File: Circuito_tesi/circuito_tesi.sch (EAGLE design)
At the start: 37 parts, among them IC1.8 317T, IC3.3 317T, IC5 317T, Q1 BSS138, U1 NRF52832, U2 SGP30, U3 MICS-6814, U4 OPA2277PA, U6 BME280, U7 LIS3DH

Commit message: Cambiate resistenze a 1/4 W max
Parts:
- removed Q1: BSS138, BSS138:BSS138
- removed R11: RMCF0603FT130R, Res_130OHM:RMCF0603FT130R
- removed R12: RMCF0603FT300R, Res_300OHM:RMCF0603FT300R
- added R8: ERA6VEB8200V, Res_820_0p25W:ERA6VEB8200V
- BT1, BT2, BT3, BT4: value BHX1-2450-SM -> 2996TR; device BHX1-2450-SM:BHX1-2450-SM -> Battery_holder:2996TR
- R1, R2: value RNCF0603BTE10K0 -> RNCP0805FTD10K0; device Res_10KOHM:RNCF0603BTE10K0 -> Res_10K_0p25W:RNCP0805FTD10K0
- R5: value RNCF0603BTE10K0 -> RP73PF2A130RBTDF; device Res_10KOHM:RNCF0603BTE10K0 -> Res_130_0p25:RP73PF2A130RBTDF
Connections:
- removed net N$8: R5.2
- net 5V: now also R5.2, R8.2; no longer R11.2, R9.2
- net GND: now also R9.1; no longer R12.1
- net N$11: now also R8.1; no longer R9.1
- net N$13: now also R5.1; no longer R11.1
- net N$9: now also R9.2; no longer R12.2
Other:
- moved on the sheet: BT1, BT2, BT3, BT4, R5, R9

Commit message: Aggiunte nuovi condensatori e voltage regulator
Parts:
- removed IC1.8, IC3.3, IC5: 317T, linear:317T
- added C7: GRM033C80J104KE15D, Condens_100nF:GRM033C80J104KE15D
- added C9: GRM033R60J103KA01D, Condens_10nF:GRM033R60J103KA01D
- added V_REG_1.8: MCP1825S-1802E/DB, V_Reg_1.8_SMD:MCP1825S-1802E/DB
- added V_REG_3.3: LD1117S33TR, V_Reg_3.3_SMD:LD1117S33TR
- added V_REG_5: LDL1117S50RSOT223_STM-L, V_Reg_5_SMD:LDL1117S50RSOT223_STM-L
- C1: value 10uF -> GRM033C80J104KE15D; device SparkFun-Capacitors:10UF-0805-10V-10% -> Condens_100nF:GRM033C80J104KE15D
- C2: value 10uF -> CL05A106MP5NUNC; device SparkFun-Capacitors:10UF-0805-10V-10% -> Condens_10uF:CL05A106MP5NUNC
- C3: value 0.33µF -> GRM035R60G475ME15D; device SparkFun-Capacitors:0.33UF/330NF-0805-50V-10% -> Condens_4.7uF:GRM035R60G475ME15D
- C4: value 0.1uF -> GRM033R60J105MEA2D; device SparkFun-Capacitors:0.1UF-0603-25V-5% -> Condens_1uF:GRM033R60J105MEA2D
- C5: value GRM033R60J103KA01D -> GRM033R60J105MEA2D; device Condens_10nF:GRM033R60J103KA01D -> Condens_1uF:GRM033R60J105MEA2D
- C6: value GRM033R60J103KA01D -> GRM035R60G475ME15D; device Condens_10nF:GRM033R60J103KA01D -> Condens_4.7uF:GRM035R60G475ME15D
- C8: value GRM033C80J104KE15D -> GRM033R60J103KA01D; device Condens_100nF:GRM033C80J104KE15D -> Condens_10nF:GRM033R60J103KA01D
- R5: value RP73PF2A130RBTDF -> RMCF0603FT5M10; device Res_130_0p25:RP73PF2A130RBTDF -> Res_5.1MOHM:RMCF0603FT5M10
- R7: value RMCF0603FT5M10 -> RP73PF2A130RBTDF; device Res_5.1MOHM:RMCF0603FT5M10 -> Res_130_0p25:RP73PF2A130RBTDF
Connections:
- net 1.8V: now also C5.2, C7.1, V_REG_1.8.VOUT; no longer C8.1, IC1.8.VO
- net 3.3: now also V_REG_3.3.OUT; no longer IC3.3.VO
- net 5V: now also C3.2, C6.2, R7.2, V_REG_1.8.VIN, V_REG_5.VOUT; no longer C4.1, IC5.VO, R5.2
- net GND: now also C1.1, C3.1, C4.1, C7.2, C8.1, C9.1, V_REG_1.8.GND_(TAB), V_REG_1.8.GND_(TAB)_2, V_REG_3.3.GND, V_REG_5.GND; no longer C1.2, C3.2, C4.2, C8.2, IC1.8.ADJ, IC3.3.ADJ, IC5.ADJ
- net N$13: now also R7.1; no longer R5.1
- net N$15: now also C9.2, R6.1; no longer C6.2, R7.1
- net N$17: now also C8.2, R5.2; no longer C5.2, R6.2
- net N$22: now also R5.1; no longer R6.1
- net N$7: now also R6.2; no longer R7.2
- net VDD: now also C1.2, C4.2, V_REG_3.3.IN, V_REG_5.VIN; no longer C1.1, C3.1, IC1.8.VI, IC3.3.VI, IC5.VI
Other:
- moved on the sheet: C1, C2, C3, C4, C5, C6, C8, R5, R6, R7

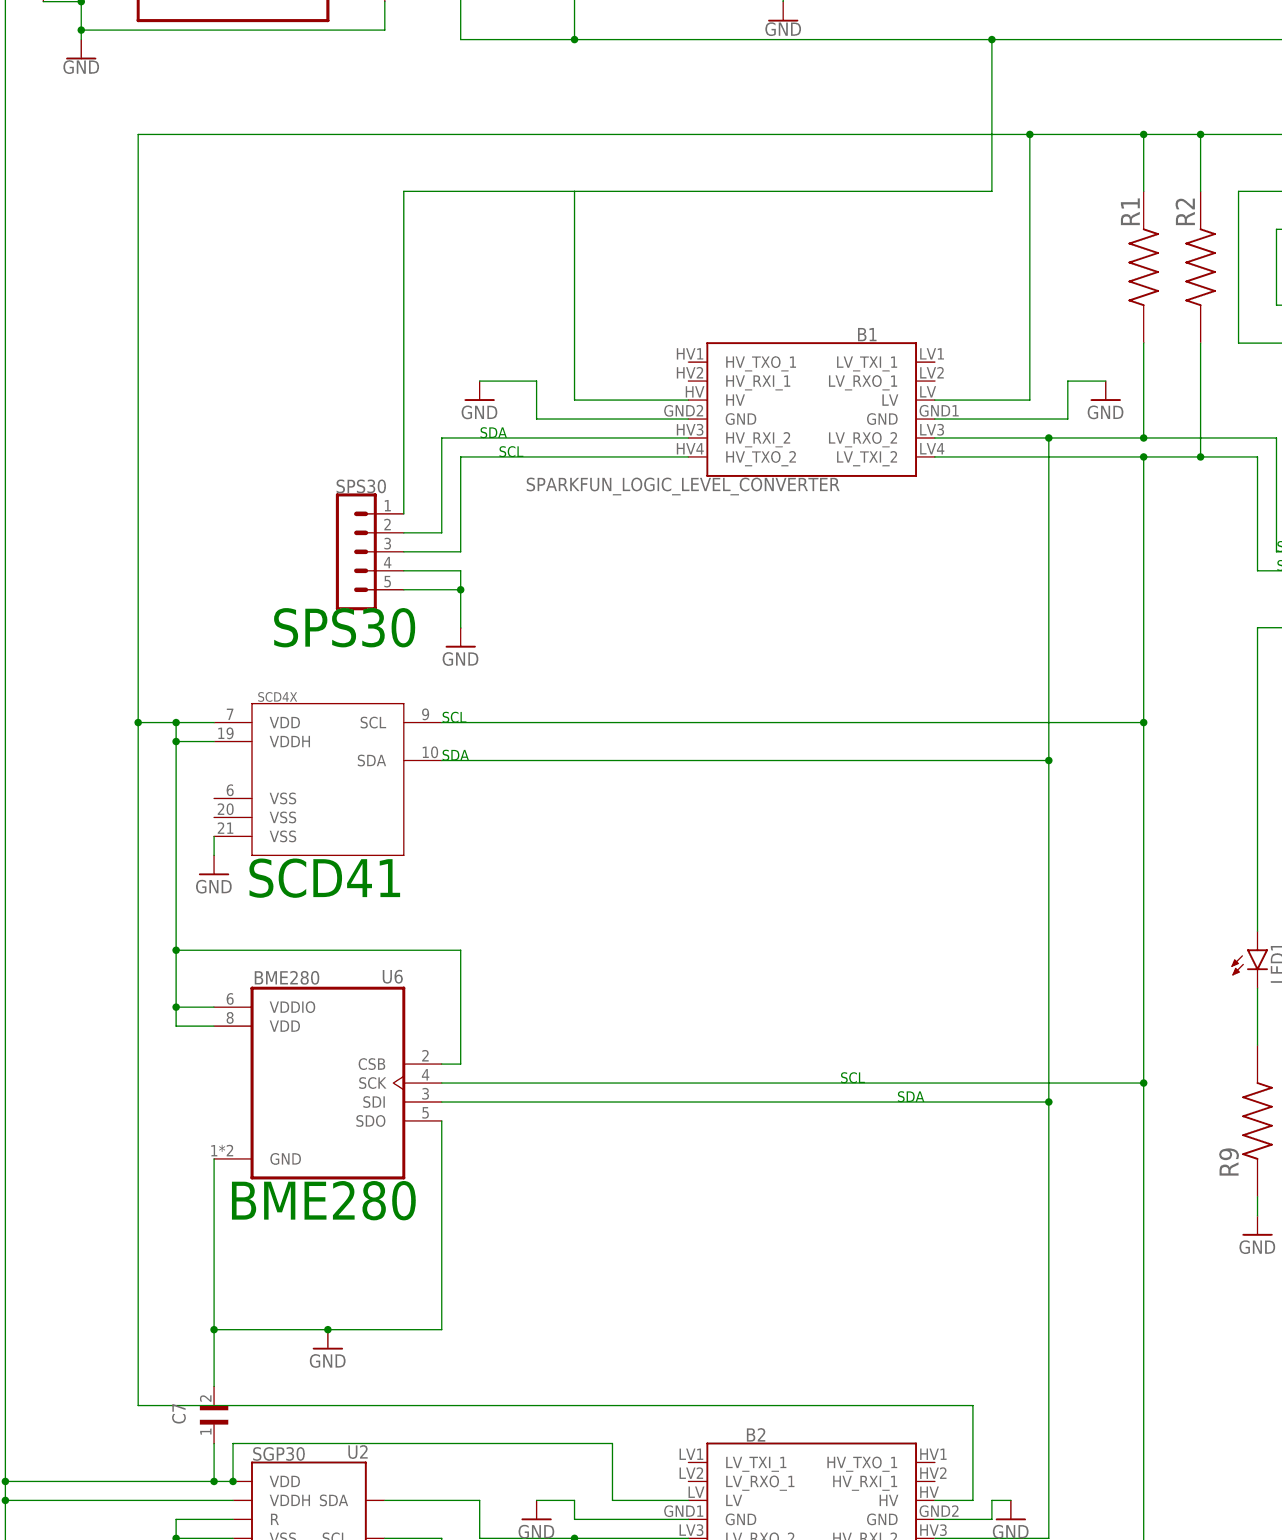
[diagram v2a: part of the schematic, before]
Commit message: Aggiunto SCD4x al circuito
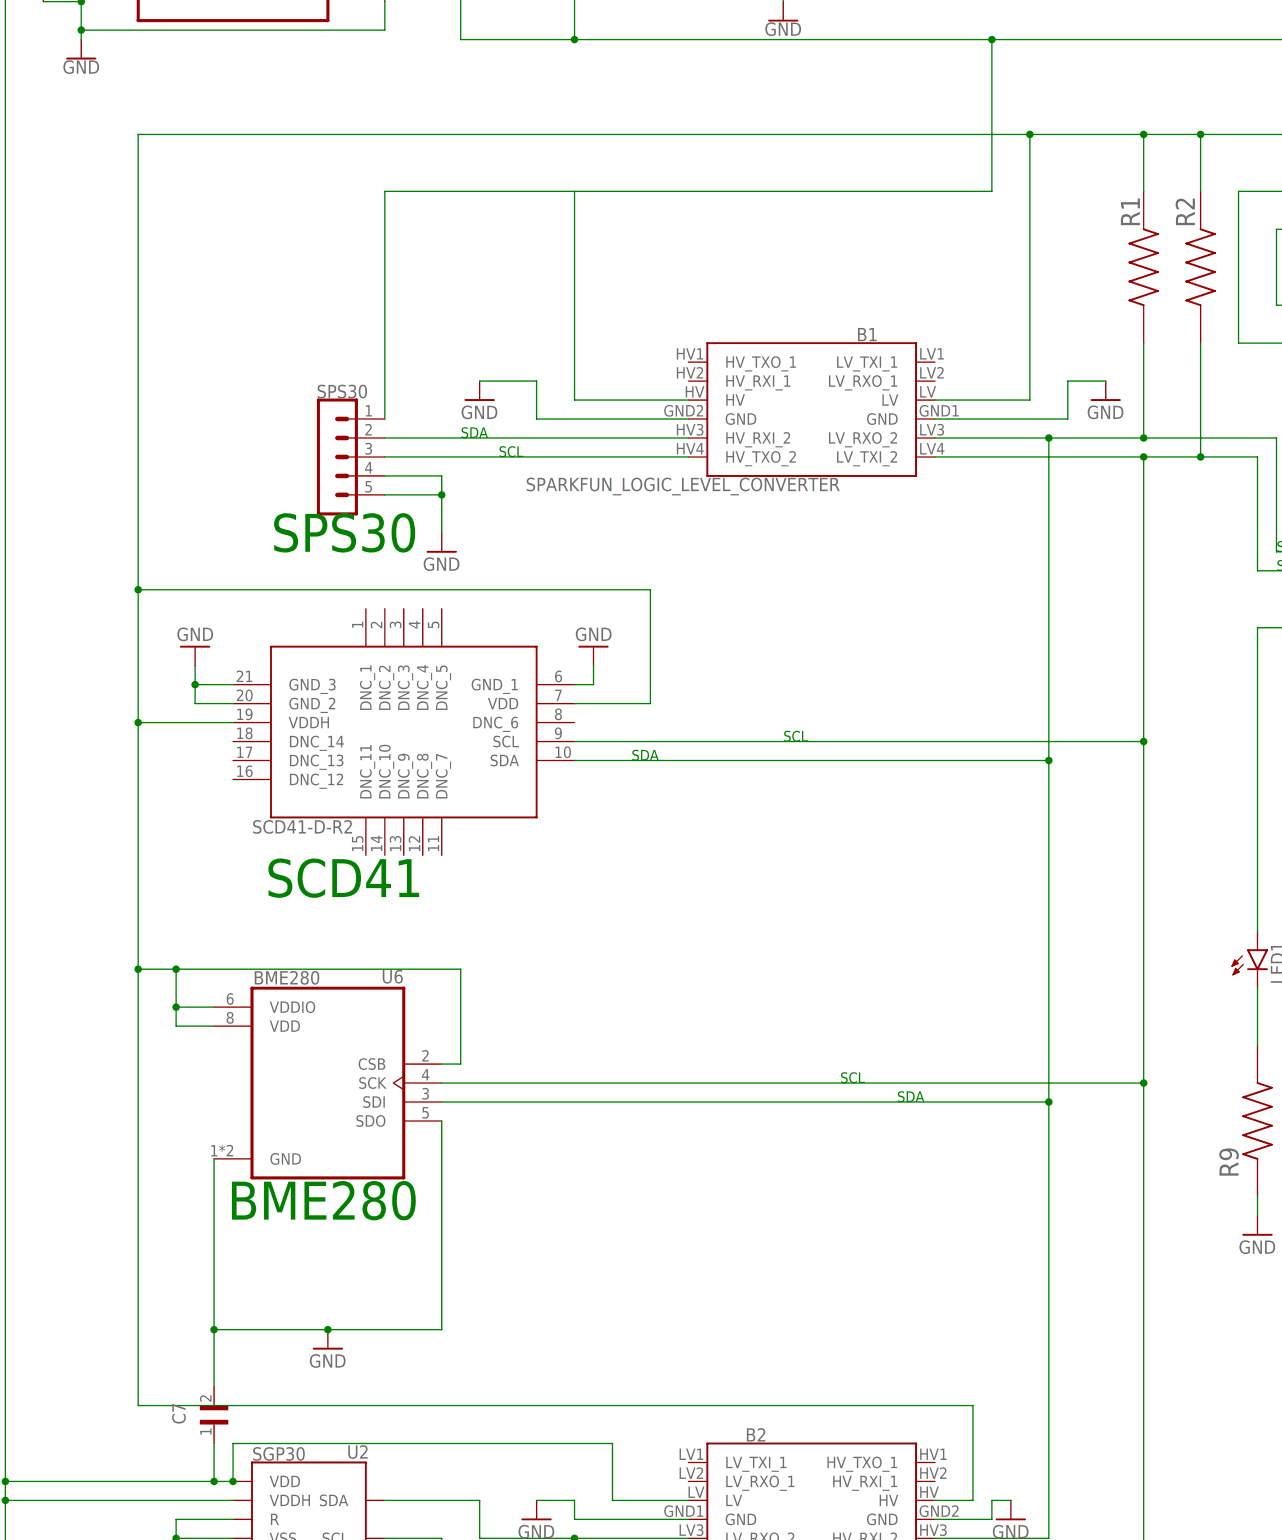
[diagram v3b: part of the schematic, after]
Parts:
- removed SCD4X: SCD4XSCD4X_SCD4X_SCD4X, SCD41-D-R1:SCD4XSCD4X_SCD4X_SCD4X
- added IC1: SCD41-D-R2, SCD41-R2_unofficial:SCD41-D-R2
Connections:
- net 3.3: now also IC1.VDD, IC1.VDDH; no longer SCD4X.VDD, SCD4X.VDDH
- net GND: now also IC1.GND_1, IC1.GND_2, IC1.GND_3; no longer SCD4X.VSS@3
- net SCL: now also IC1.SCL; no longer SCD4X.SCL
- net SDA: now also IC1.SDA; no longer SCD4X.SDA
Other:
- moved on the sheet: SPS30
